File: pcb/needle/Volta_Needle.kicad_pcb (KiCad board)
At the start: 2 copper layers, 45.8 x 17.9 mm, 2 parts, among them J1 Arm, J2 Needle

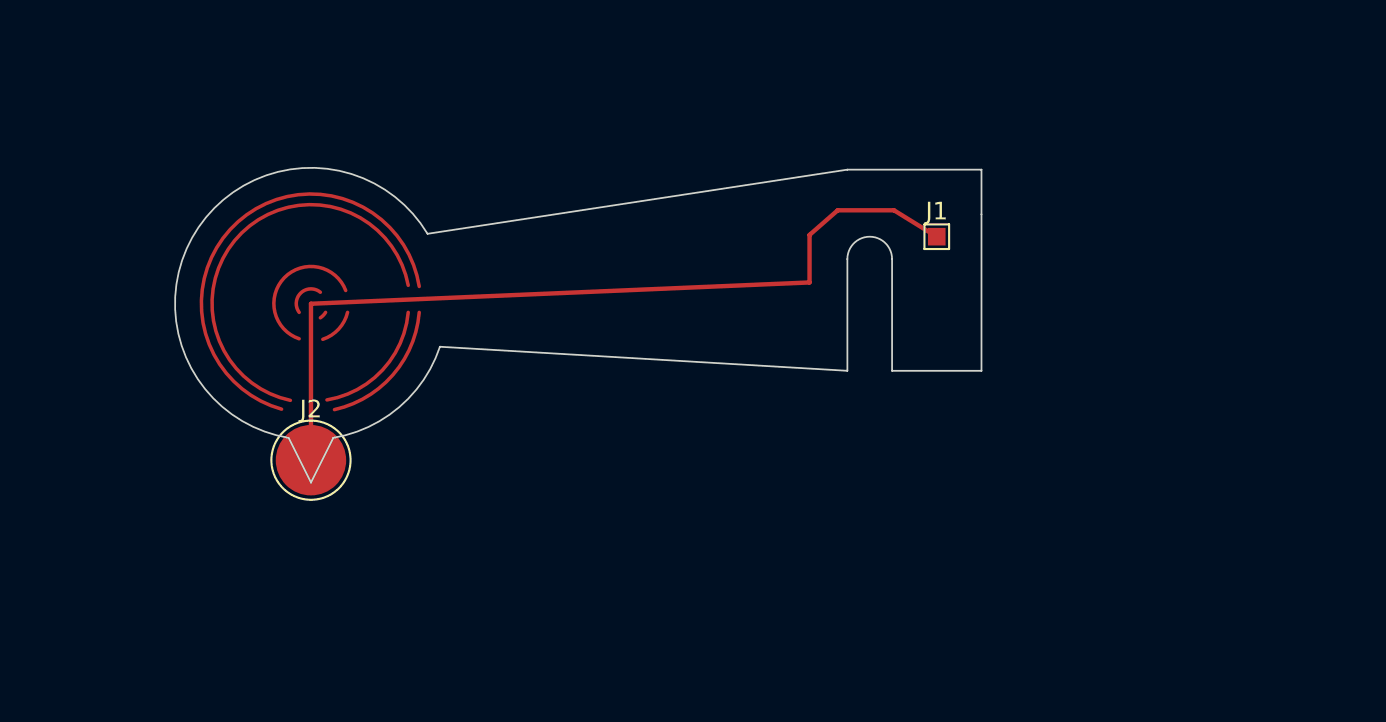
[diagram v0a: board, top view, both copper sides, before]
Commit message: changes volta needle to spec
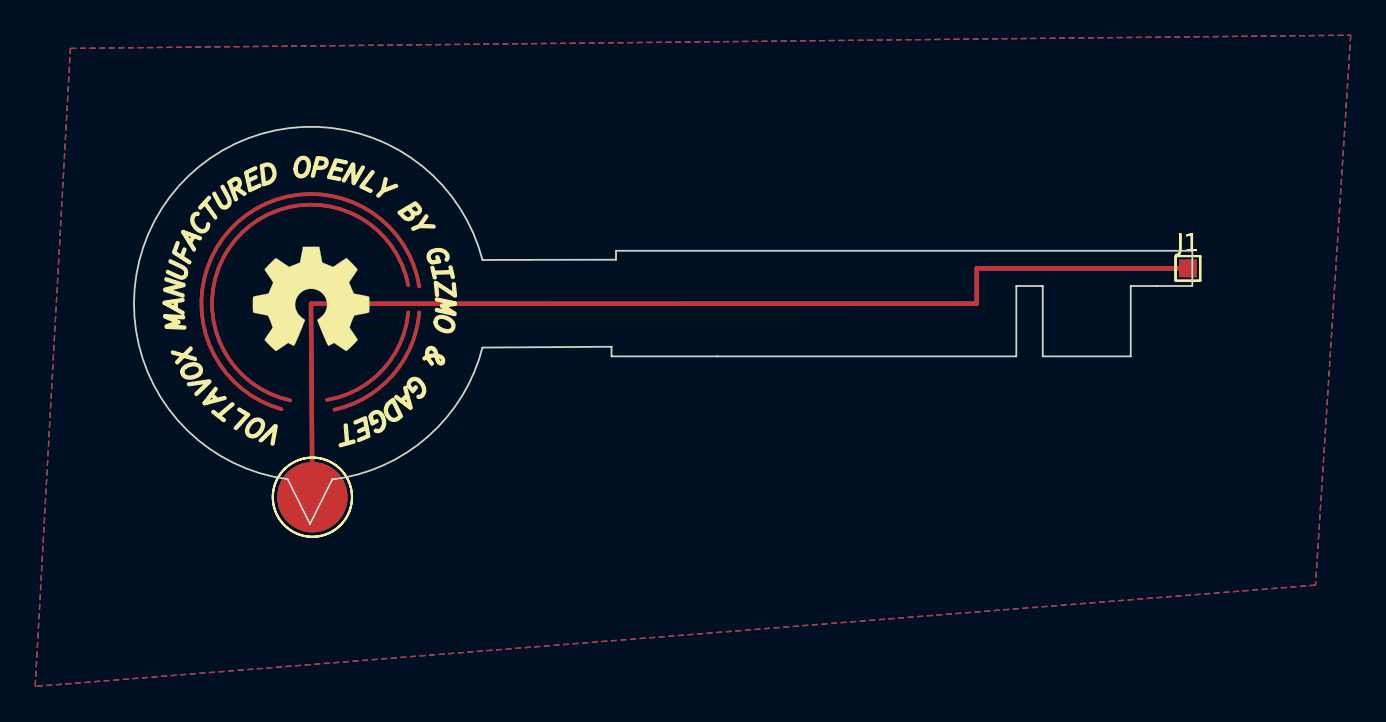
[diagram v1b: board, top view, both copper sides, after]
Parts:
- removed the J1 at (189.2, 76.2)
- added J1 (x2): Arm, TestPoint:TestPoint_Pad_1.0x1.0mm, F.Cu at (203.5, 78.0)
- added J2: Needle, TestPoint:TestPoint_Pad_D4.0mm, F.Cu at (153.8, 91.0)
- added REF**: OSHW-Symbol_6.7x6mm_SilkScreen, Symbol:OSHW-Symbol_6.7x6mm_SilkScreen, F.Cu at (153.7, 79.8)
- added REF**: OSHW-Symbol_6.7x6mm_SilkScreen, Symbol:OSHW-Symbol_6.7x6mm_SilkScreen, B.Cu at (153.7, 79.8)
- moved J2 2.10 mm to (153.8, 91.0)
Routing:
- net Net-(J1-Pad1): track 48.1 -> 125.6 mm
- added copper zone on B.Cu, net (none)
- added copper zone on F.Cu, net (none)
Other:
- board size 45.8 x 17.9 mm -> 60.1 x 22.6 mm

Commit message: updates length of needle pcb
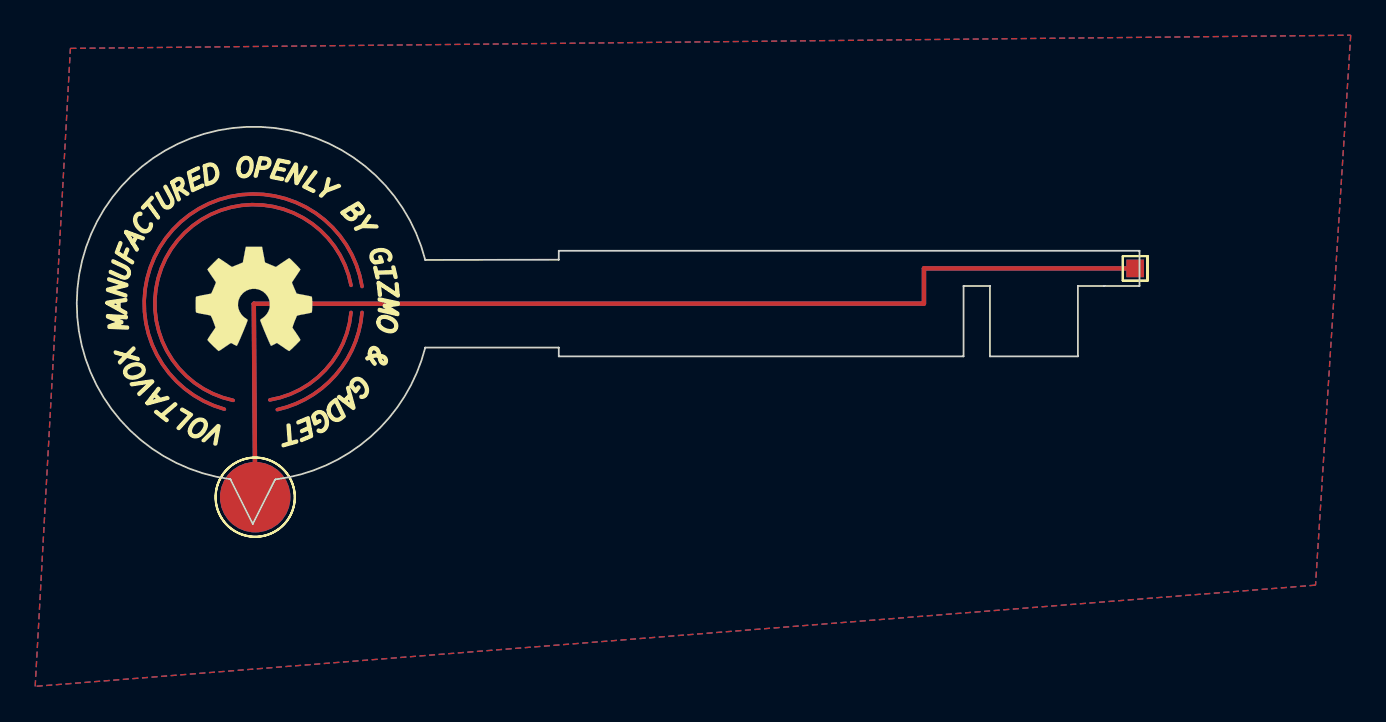
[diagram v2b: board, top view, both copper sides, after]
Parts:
- moved J2 3.25 mm to (150.5, 91.0) (x2)
- moved REF** 3.25 mm to (150.4, 79.8) (x2)
- moved J1 3.00 mm to (200.5, 78.0) (x2)
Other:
- board size 60.1 x 22.6 mm -> 60.4 x 22.6 mm

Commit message: updates length of needle pcb
again
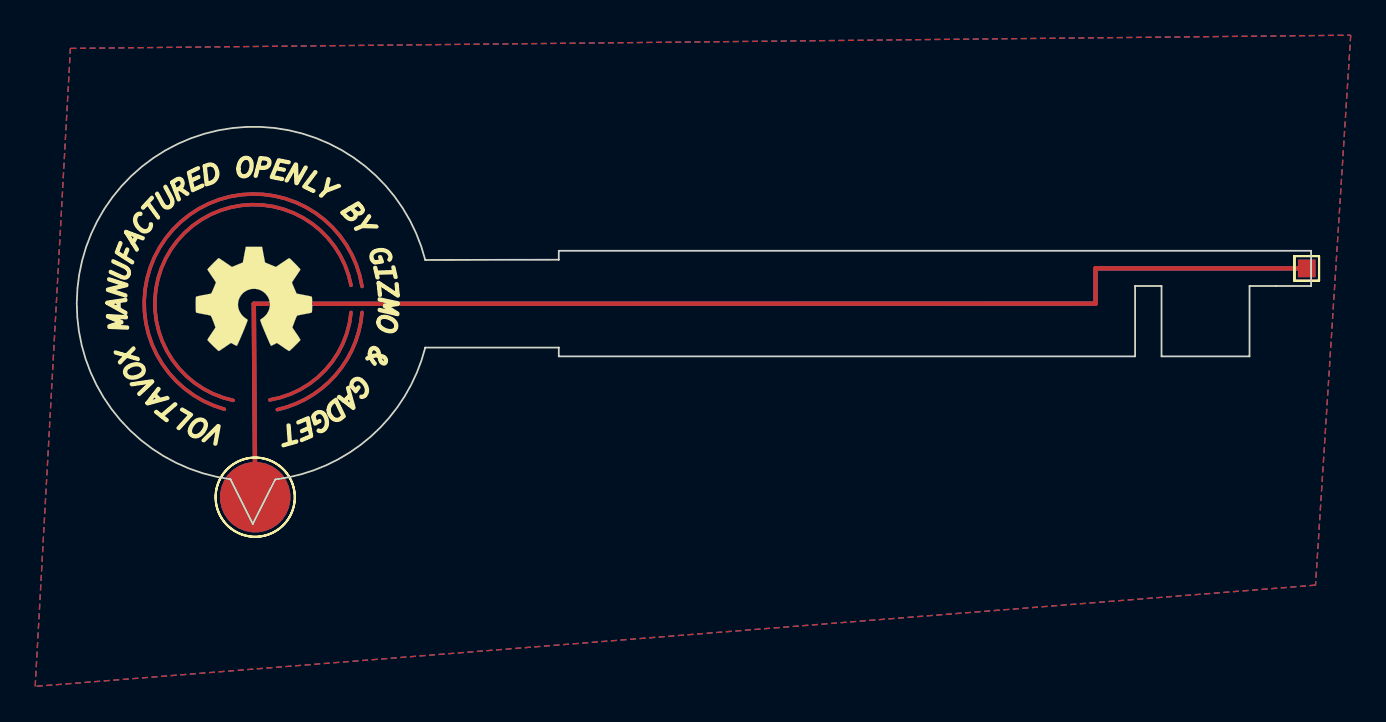
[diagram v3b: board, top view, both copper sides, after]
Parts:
- moved J1 9.75 mm to (210.2, 78.0)
- moved J1 9.75 mm to (210.3, 78.0)
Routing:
- net Net-(J1-Pad1): track 126.1 -> 145.6 mm
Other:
- board size 60.4 x 22.6 mm -> 70.1 x 22.6 mm
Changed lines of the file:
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@@
   (net 1 "Net-(J1-Pad1)")
   (footprint "TestPoint:TestPoint_Pad_1.0x1.0mm" (layer "F.Cu")
-    (at 200.5 78)
+    (at 210.25 78)
     (descr "SMD rectangular pad as test Point, square 1.0mm side length")
     (tags "test point SMD pad rectangle square")
@@
   )
   (footprint "TestPoint:TestPoint_Pad_1.0x1.0mm" (layer "F.Cu")
-    (at 200.502049 78.002299)
+    (at 210.252049 78.002299)
     (descr "SMD rectangular pad as test Point, square 1.0mm side length")
     (tags "test point SMD pad rectangle square")
@@
       (xy 148.388338 86.935923)
     ) (layer "F.SilkS") (width 0.2) (fill solid))
-  (gr_line (start 190.75 79) (end 190.75 83) (layer "Edge.Cuts") (width 0.1))
-  (gr_line (start 192.25 79) (end 190.75 79) (layer "Edge.Cuts") (width 0.1))
-  (gr_line (start 200.75 77) (end 200.75 79) (layer "Edge.Cuts") (width 0.1))
-  (gr_line (start 190.75 83) (end 167.75 83) (layer "Edge.Cuts") (width 0.1))
+  (gr_line (start 150.5 80) (end 200.5 80) (layer "Dwgs.User") (width 0.15))
+  (gr_line (start 200.5 79) (end 200.5 83) (layer "Edge.Cuts") (width 0.1))
+  (gr_line (start 202 79) (end 200.5 79) (layer "Edge.Cuts") (width 0.1))
+  (gr_line (start 210.5 77) (end 210.5 79) (layer "Edge.Cuts") (width 0.1))
   (gr_line (start 160.164993 82.5) (end 167.75 82.5) (layer "Edge.Cuts") (width 0.1))
   (gr_line (start 149.095 89.98) (end 150.365 92.52) (layer "Edge.Cuts") (width 0.1))
+  (gr_line (start 167.75 77) (end 210.5 77) (layer "Edge.Cuts") (width 0.1))
   (gr_line (start 160.164994 77.521705) (end 167.75 77.507364) (layer "Edge.Cuts") (width 0.1))
   (gr_arc (start 160.164993 82.5) (mid 157.059327 87.565417) (end 151.636732 89.994215) (layer "Edge.Cuts") (width 0.1))
-  (gr_line (start 192.25 83) (end 197.25 83) (layer "Edge.Cuts") (width 0.1))
-  (gr_line (start 167.75 77) (end 200.75 77) (layer "Edge.Cuts") (width 0.1))
-  (gr_line (start 198.75 79) (end 200.75 79) (layer "Edge.Cuts") (width 0.1))
-  (gr_line (start 197.25 83) (end 197.25 79) (layer "Edge.Cuts") (width 0.1))
+  (gr_line (start 202 83) (end 207 83) (layer "Edge.Cuts") (width 0.1))
+  (gr_line (start 167.75 83) (end 200.5 83) (layer "Edge.Cuts") (width 0.1))
+  (gr_line (start 208.5 79) (end 210.5 79) (layer "Edge.Cuts") (width 0.1))
+  (gr_line (start 207 83) (end 207 79) (layer "Edge.Cuts") (width 0.1))
   (gr_arc (start 149.095 89.98) (mid 142.901599 73.329418) (end 160.164994 77.521705) (layer "Edge.Cuts") (width 0.1))
-  (gr_line (start 192.25 83) (end 192.25 79) (layer "Edge.Cuts") (width 0.1))
-  (gr_line (start 197.25 79) (end 198.75 79) (layer "Edge.Cuts") (width 0.1))
+  (gr_line (start 202 83) (end 202 79) (layer "Edge.Cuts") (width 0.1))
+  (gr_line (start 207 79) (end 208.5 79) (layer "Edge.Cuts") (width 0.1))
   (gr_line (start 167.75 77) (end 167.75 77.507364) (layer "Edge.Cuts") (width 0.1))
   (gr_line (start 167.75 82.5) (end 167.75 83) (layer "Edge.Cuts") (width 0.1))
   (gr_line (start 150.365 92.52) (end 151.636732 89.994215) (layer "Edge.Cuts") (width 0.1))
-  (segment (start 188.5 80) (end 150.42 80.01) (width 0.25) (layer "F.Cu") (net 1))
-  (segment (start 200.5 78) (end 188.5 78) (width 0.25) (layer "F.Cu") (net 1))
+  (segment (start 198.25 80) (end 150.42 80.01) (width 0.25) (layer "F.Cu") (net 1))
+  (segment (start 210.25 78) (end 198.25 78) (width 0.25) (layer "F.Cu") (net 1))
   (segment (start 150.42 80.01) (end 150.5 91) (width 0.25) (layer "F.Cu") (net 1))
-  (segment (start 188.5 80) (end 188.5 78) (width 0.25) (layer "F.Cu") (net 1))
-  (segment (start 150.422049 80.012299) (end 188.502049 80.002299) (width 0.25) (layer "B.Cu") (net 1))
+  (segment (start 198.25 80) (end 198.25 78) (width 0.25) (layer "F.Cu") (net 1))
   (segment (start 150.422049 80.012299) (end 150.502049 91.002299) (width 0.25) (layer "B.Cu") (net 1))
-  (segment (start 200.502049 78.002299) (end 188.502049 78.002299) (width 0.25) (layer "B.Cu") (net 1))
-  (segment (start 188.502049 80.002299) (end 188.502049 78.002299) (width 0.25) (layer "B.Cu") (net 1))
+  (segment (start 210.252049 78.002299) (end 198.252049 78.002299) (width 0.25) (layer "B.Cu") (net 1))
+  (segment (start 198.252049 80.002299) (end 198.252049 78.002299) (width 0.25) (layer "B.Cu") (net 1))
+  (segment (start 150.422049 80.012299) (end 198.252049 80.002299) (width 0.25) (layer "B.Cu") (net 1))
   (zone (net 0) (net_name "") (layers F&B.Cu) (hatch edge 0.508)
     (connect_pads (clearance 0))

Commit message: tweaks aesthetic things about the horn pcbs
send Rev0 to JLC for manufacturing
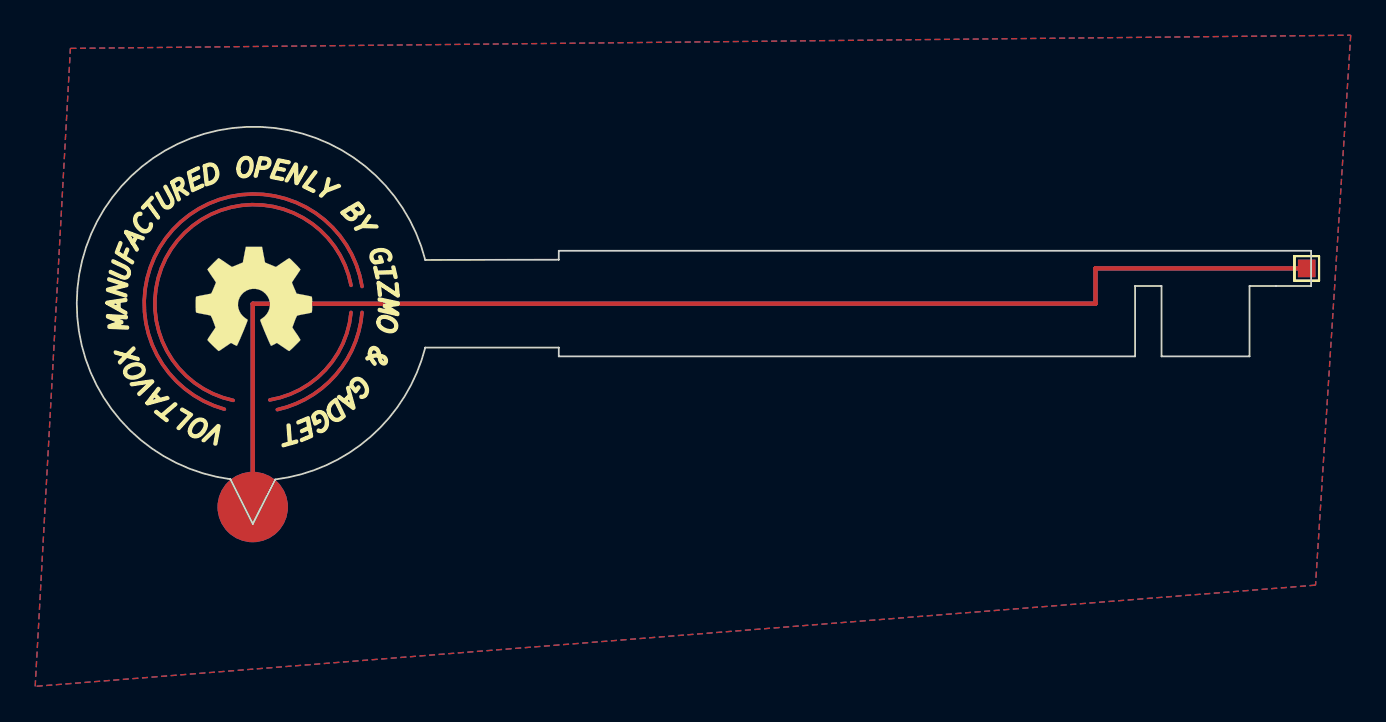
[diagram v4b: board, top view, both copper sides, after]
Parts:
- moved J2 0.58 mm to (150.4, 91.6) (x2)
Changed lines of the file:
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@@
       (sketchpadsonfab false)
       (subtractmaskfromsilk false)
-      (outputformat 3)
+      (outputformat 1)
       (mirror false)
       (drillshape 0)
       (scaleselection 1)
-      (outputdirectory "../../../../../Downloads/")
+      (outputdirectory "Rev0/")
     )
   )
@@
     (fp_line (start 1 1) (end -1 1) (layer "F.CrtYd") (width 0.05))
     (fp_line (start -1 -1) (end -1 1) (layer "F.CrtYd") (width 0.05))
-    (pad "1" smd rect (at 0 0) (size 1 1) (layers "F.Cu" "F.Mask")
+    (pad "1" smd rect (at 0 0) (size 1 1) (layers *.Mask "F.Cu")
       (net 1 "Net-(J1-Pad1)") (pinfunction "Pin_1") (pintype "passive"))
   )
   (footprint "TestPoint:TestPoint_Pad_D4.0mm" (layer "F.Cu")
-    (at 150.502049 91.002299)
+    (at 150.36 91.56)
     (descr "SMD pad as test Point, diameter 4.0mm")
     (tags "test point SMD pad")
@@
       (effects (font (size 1 1) (thickness 0.15)))
     )
-    (fp_circle (center 0 0) (end 0 2.25) (layer "F.SilkS") (width 0.12) (fill none))
     (fp_circle (center 0 0) (end 2.5 0) (layer "F.CrtYd") (width 0.05) (fill none))
-    (pad "1" smd circle (at 0 0) (size 4 4) (layers "B.Cu" "F.Mask")
+    (pad "1" smd circle (at 0 0) (size 4 4) (layers *.Mask "B.Cu")
       (net 1 "Net-(J1-Pad1)") (pinfunction "Pin_1") (pintype "passive"))
   )
   (footprint "TestPoint:TestPoint_Pad_D4.0mm" (layer "F.Cu")
-    (at 150.5 91)
+    (at 150.36 91.56)
     (descr "SMD pad as test Point, diameter 4.0mm")
     (tags "test point SMD pad")
@@
       (effects (font (size 1 1) (thickness 0.15)))
     )
-    (fp_circle (center 0 0) (end 0 2.25) (layer "F.SilkS") (width 0.12) (fill none))
     (fp_circle (center 0 0) (end 2.5 0) (layer "F.CrtYd") (width 0.05) (fill none))
     (pad "1" smd circle (at 0 0) (size 4 4) (layers "F.Cu" "F.Mask")
@@
   (gr_line (start 167.75 82.5) (end 167.75 83) (layer "Edge.Cuts") (width 0.1))
   (gr_line (start 150.365 92.52) (end 151.636732 89.994215) (layer "Edge.Cuts") (width 0.1))
-  (segment (start 198.25 80) (end 150.42 80.01) (width 0.25) (layer "F.Cu") (net 1))
+  (segment (start 150.36 90.86) (end 150.5 91) (width 0.25) (layer "F.Cu") (net 1))
+  (segment (start 150.36 80.01) (end 150.36 90.86) (width 0.25) (layer "F.Cu") (net 1))
   (segment (start 210.25 78) (end 198.25 78) (width 0.25) (layer "F.Cu") (net 1))
-  (segment (start 150.42 80.01) (end 150.5 91) (width 0.25) (layer "F.Cu") (net 1))
-  (segment (start 198.25 80) (end 198.25 78) (width 0.25) (layer "F.Cu") (net 1))
-  (segment (start 150.422049 80.012299) (end 150.502049 91.002299) (width 0.25) (layer "B.Cu") (net 1))
+  (segment (start 198.25 80) (end 150.36 80.01) (width 0.25) (layer "F.Cu") (net 1))
+  (segment (start 198.25 78) (end 198.25 80) (width 0.25) (layer "F.Cu") (net 1))
+  (segment (start 198.252049 78.002299) (end 198.252049 80.002299) (width 0.25) (layer "B.Cu") (net 1))
   (segment (start 210.252049 78.002299) (end 198.252049 78.002299) (width 0.25) (layer "B.Cu") (net 1))
-  (segment (start 198.252049 80.002299) (end 198.252049 78.002299) (width 0.25) (layer "B.Cu") (net 1))
-  (segment (start 150.422049 80.012299) (end 198.252049 80.002299) (width 0.25) (layer "B.Cu") (net 1))
+  (segment (start 198.252049 80.002299) (end 150.36 80.012299) (width 0.25) (layer "B.Cu") (net 1))
+  (segment (start 150.36 80.012299) (end 150.36 90.86025) (width 0.25) (layer "B.Cu") (net 1))
+  (segment (start 150.36 90.86025) (end 150.502049 91.002299) (width 0.25) (layer "B.Cu") (net 1))
   (zone (net 0) (net_name "") (layers F&B.Cu) (hatch edge 0.508)
     (connect_pads (clearance 0))
